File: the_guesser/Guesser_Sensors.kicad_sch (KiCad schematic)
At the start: 1 part, among them U8 MS5607-02BA

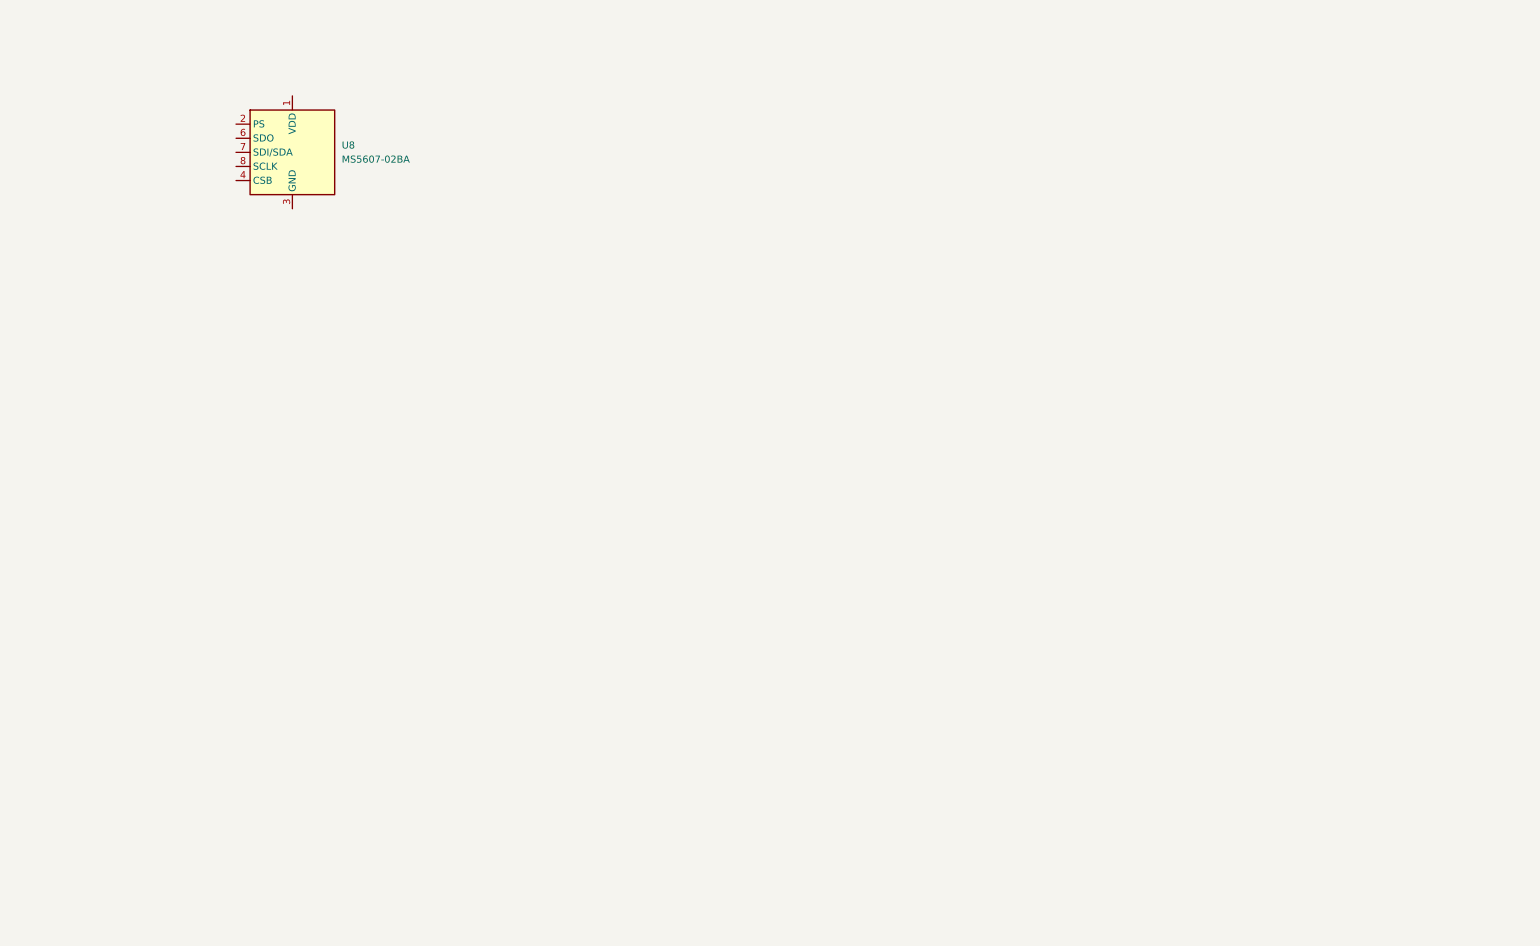
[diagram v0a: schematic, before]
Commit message: Started Guesser I/O and continued sensor selection
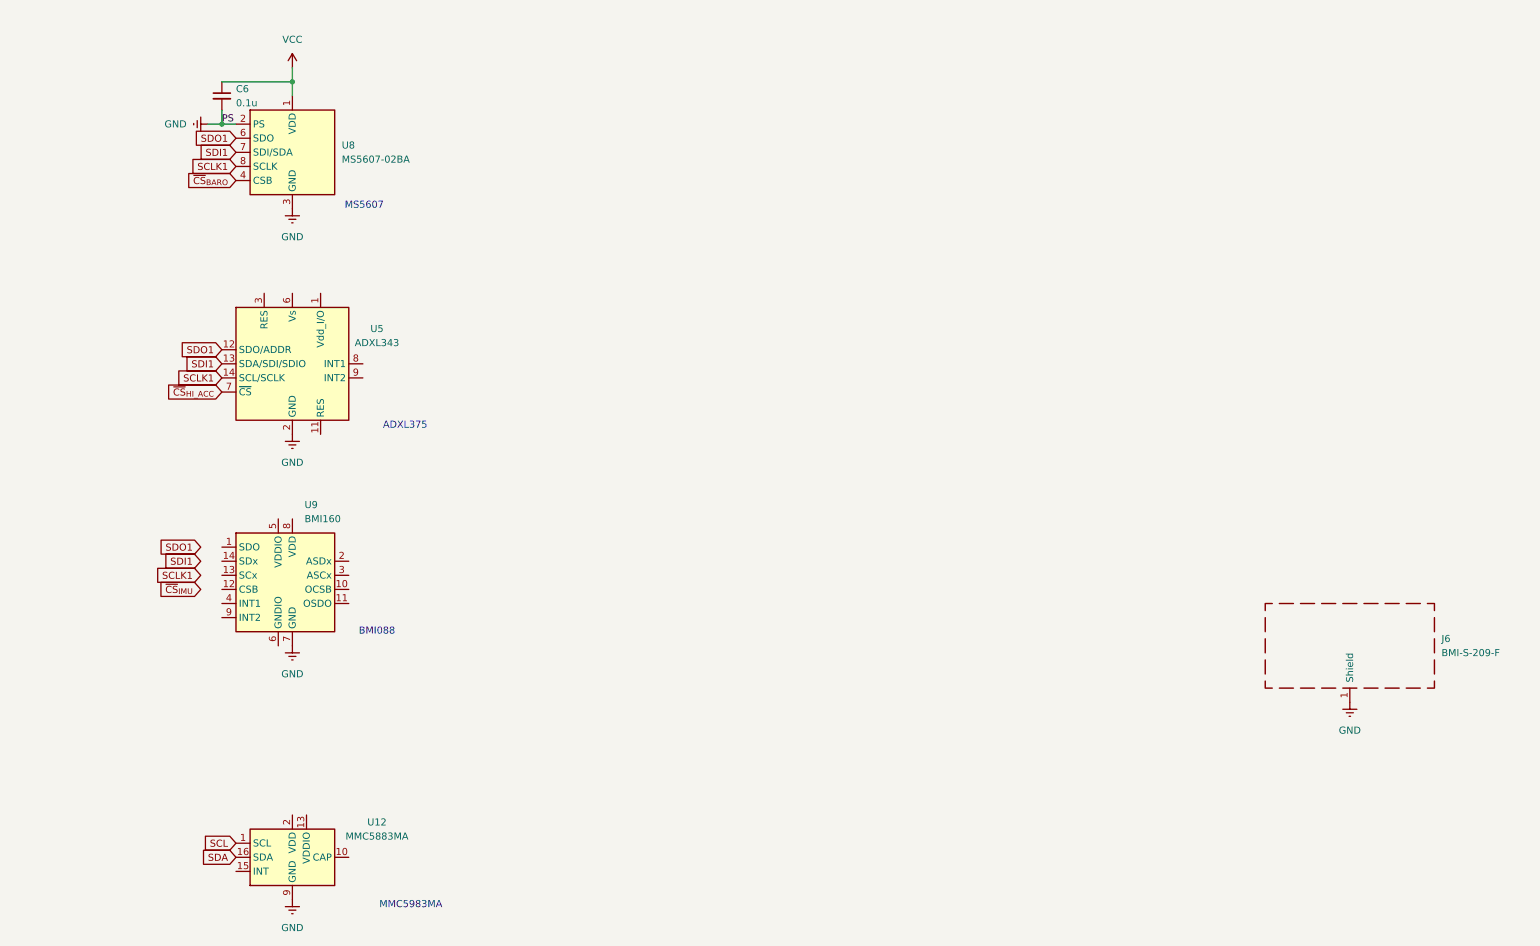
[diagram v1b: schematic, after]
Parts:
- added C6: 0.1u, Capacitor_SMD:C_0603_1608Metric, symbol Device:C_Small
- added J6: BMI-S-209-F, RF_Shielding:Laird_Technologies_BMI-S-209-F_29.36x18.50mm, symbol Device:RFShield_OnePiece
- added U12: MMC5883MA, Package_LGA:LGA-16_3x3mm_P0.5mm, symbol Sensor_Magnetic:MMC5883MA
- added U5: ADXL343, Package_LGA:LGA-14_3x5mm_P0.8mm_LayoutBorder1x6y, symbol Sensor_Motion:ADXL343
- added U9: BMI160, Package_LGA:Bosch_LGA-14_3x2.5mm_P0.5mm, symbol Sensor_Motion:BMI160
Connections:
- net VCC: now reaches U8.1 (VDD)
- net VCC: now also C6.1
- net GND: now reaches U8.2 (PS)
- net GND: now also U8.3 (GND), C6.2, J6.1 (Shield), U12.11 (GND), U12.9 (GND), U5.2 (GND), U5.4 (GND), U5.5 (GND), U9.7 (GND)
- net ~{CS}_{BARO}: now reaches U8.4 (CSB), U8.5 (CSB)
- net SDO1: now reaches U8.6 (SDO)
- net SDO1: now also U5.12 (SDO/ADDR)
- net SDI1: now reaches U8.7 (SDI/SDA)
- net SDI1: now also U5.13 (SDA/SDI/SDIO)
- net SCLK1: now reaches U8.8 (SCLK)
- net SCLK1: now also U5.14 (SCL/SCLK)
- new net SCL: U12.1 (SCL)
- new net SDA: U12.16 (SDA)
- new net ~{CS}_{HI_ACC}: U5.7 (~{CS})
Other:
- note added: "ADXL375"
- note added: "BMI088"
- note added: "MMC5983MA"
- note added: "MS5607"

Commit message: Finished Guesser sensor selection and started sensor routing
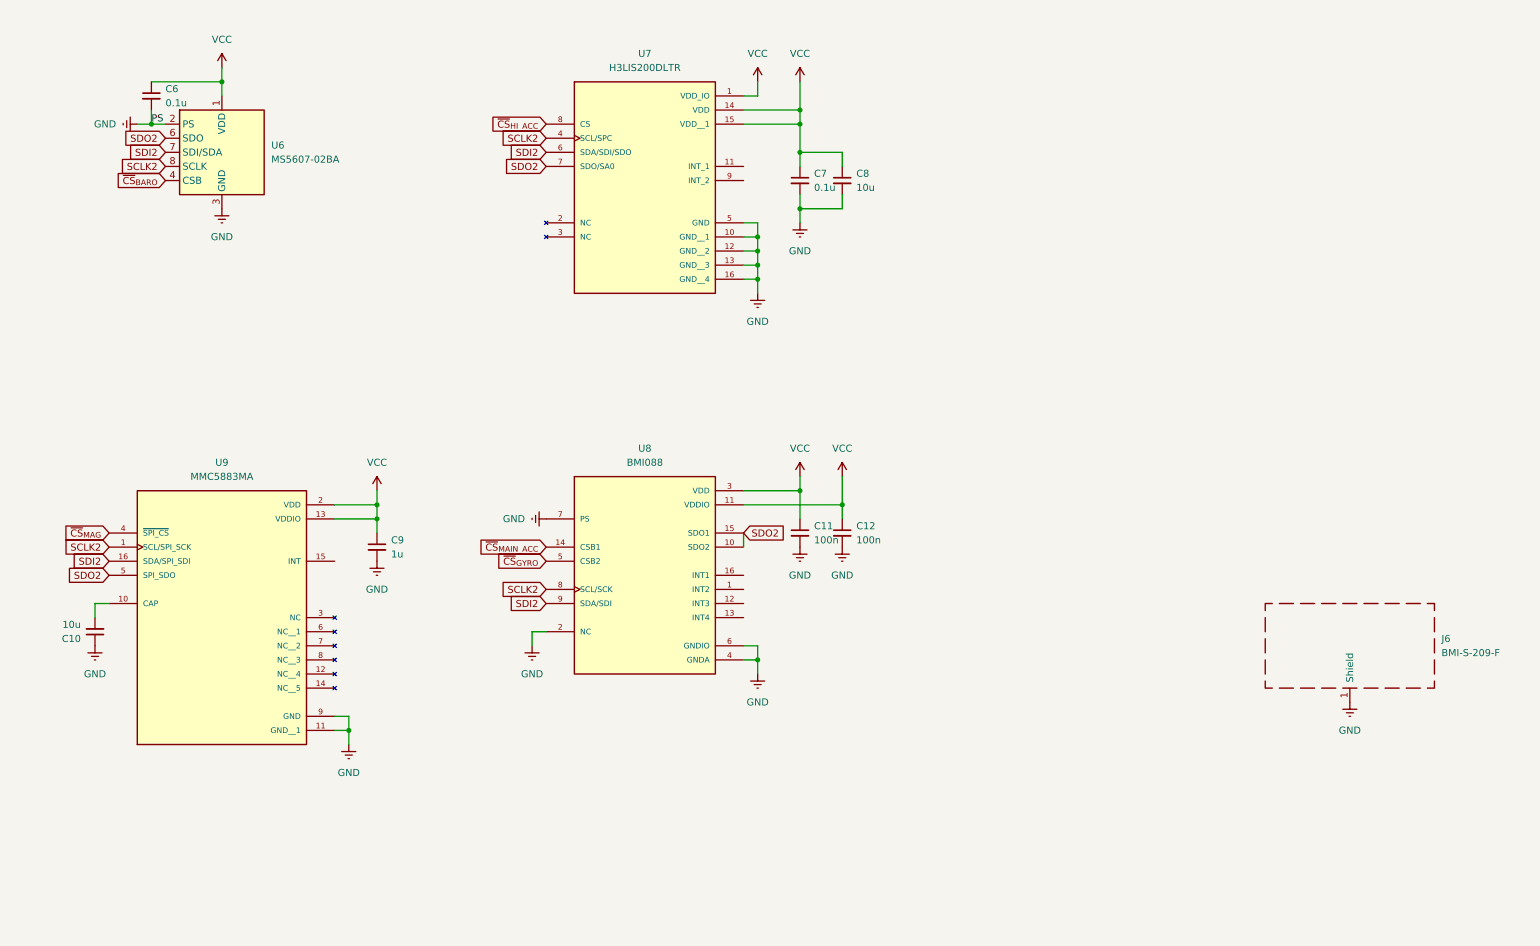
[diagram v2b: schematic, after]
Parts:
- removed U5: ADXL343, Package_LGA:LGA-14_3x5mm_P0.8mm_LayoutBorder1x6y, symbol Sensor_Motion:ADXL343
- added C10, C8: 10u, Capacitor_SMD:C_0603_1608Metric, symbol Device:C_Small
- added C11, C12: 100n, Capacitor_SMD:C_0603_1608Metric, symbol Device:C_Small
- added C7: 0.1u, Capacitor_SMD:C_0603_1608Metric, symbol Device:C_Small
- added C9: 1u, Capacitor_SMD:C_0603_1608Metric, symbol Device:C_Small
- added U7: H3LIS200DLTR, locals_but_working_PLEASE:H3LIS200DLTR, symbol Custom_Flight_Computer_Symbols:H3LIS200DLTR
- U8: renamed from U9; value BMI160 -> BMI088; footprint Package_LGA:Bosch_LGA-14_3x2.5mm_P0.5mm -> locals_but_working_PLEASE:BMI088; symbol Sensor_Motion:BMI160 -> Custom_Flight_Computer_Symbols:BMI088; AVAILABILITY (none) -> In Stock; DKPN (none) -> 828-1082-1-ND; MF (none) -> Bosch Sensortec; MP (none) -> BMI088; PACKAGE (none) -> VFLGA-16 Bosch Sensortec; PRICE (none) -> None; PURCHASE-URL (none) -> https://pricing.snapeda.com/search/part/BMI088/?ref=eda
- U9: renamed from U12; footprint Package_LGA:LGA-16_3x3mm_P0.5mm -> locals_but_working_PLEASE:MMC5983MA; symbol Sensor_Magnetic:MMC5883MA -> Custom_Flight_Computer_Symbols:MMC5983MA; DKPN (none) -> 1267-MMC5983MACT-ND; MANUFACTURER (none) -> Memsic Inc.; MAXIMUM_PACKAGE_HEIGHT (none) -> 1.00 mm; PARTREV (none) -> A; STANDARD (none) -> IPC 7351B
- renumbered U8 to U6
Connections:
- net SCL is gone; now on net SCLK2: U9.1 (SCL/SPI_SCK)
- net SCLK1 is gone; now on net SCLK2: U6.8 (SCLK)
- net SDA is gone; now on net SDI2: U9.16 (SDA/SPI_SDI)
- net SDI1 is gone; now on net SDI2: U6.7 (SDI/SDA)
- net SDO1 is gone; now on net SDO2: U6.6 (SDO)
- net GND: now also U8.2 (NC), U8.4 (GNDA), U8.6 (GNDIO), C10.1, C11.2, C12.2, C7.2, C8.2, C9.2, U7.10 (GND__1), U7.12 (GND__2), U7.13 (GND__3), U7.16 (GND__4), U7.5 (GND)
- net VCC: now also U8.11 (VDDIO), U8.3 (VDD), U9.13 (VDDIO), U9.2 (VDD), C11.1, C12.1, C7.1, C8.1, C9.1, U7.1 (VDD_IO), U7.14 (VDD), U7.15 (VDD__1)
- net ~{CS}_{HI_ACC}: now also U7.8 (CS)
- net SDO2: now reaches U8.10 (SDO2)
- net SDO2: now also U8.15 (SDO1), U9.5 (SPI_SDO), U7.7 (SDO/SA0)
- net ~{CS}_{MAIN_ACC}: now reaches U8.14 (CSB1)
- net ~{CS}_{GYRO}: now reaches U8.5 (CSB2)
- net SCLK2: now reaches U8.8 (SCL/SCK)
- net SCLK2: now also U7.4 (SCL/SPC)
- net SDI2: now reaches U8.9 (SDA/SDI)
- net SDI2: now also U7.6 (SDA/SDI/SDO)
- net at U9.10 (CAP): now also C10.2
- net ~{CS}_{MAG}: now reaches U9.4 (~{SPI_CS})
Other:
- note removed: "ADXL375"
- note removed: "BMI088"
- note removed: "MMC5983MA"
- note removed: "MS5607"
- moved on the sheet: C6, U6

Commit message: Routed USB and SPI buses
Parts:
- added U11: SAM-M8Q, RF_GPS:ublox_SAM-M8Q, symbol RF_GPS:SAM-M8Q
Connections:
- net GND: now also U11.1 (GND), U11.10 (GND), U11.11 (GND), U11.15 (GND), U11.16 (GND), U11.20 (GND), U11.4 (GND), U11.5 (GND), U11.6 (GND)
- net VCC: now also U11.17 (VCC), U11.2 (VCC_IO), U11.3 (V_BCKP)
- new net SCL1: U11.12 (SCL)
- new net SDA1: U11.9 (SDA)
- no-connect marks 0 -> 6

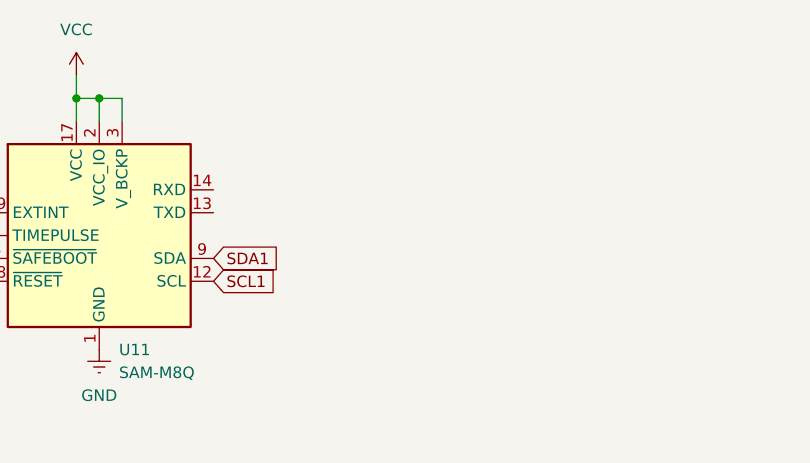
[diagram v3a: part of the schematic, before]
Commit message: Finished routing Timer Programmer
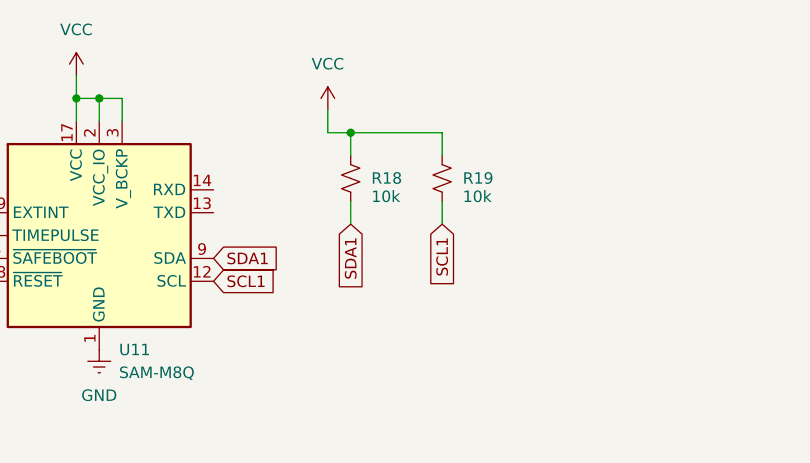
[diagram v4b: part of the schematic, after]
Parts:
- added R18, R19: 10k, Resistor_SMD:R_0603_1608Metric, symbol Device:R_Small_US
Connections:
- net SCL1: now also R19.2
- net SDA1: now also R18.2
- net VCC: now also R18.1, R19.1

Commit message: Updated Guesser USB and GPS
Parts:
- removed R18, R19: 10k, Resistor_SMD:R_0603_1608Metric, symbol Device:R_Small_US
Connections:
- net SCL1: no longer U11.12 (SCL)
- net SDA1: no longer U11.9 (SDA)
- net TXD: now reaches U11.13 (TXD)
- net RXD: now reaches U11.14 (RXD)
- no-connect marks 6 -> 8
